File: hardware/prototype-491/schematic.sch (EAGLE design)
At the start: 10 parts

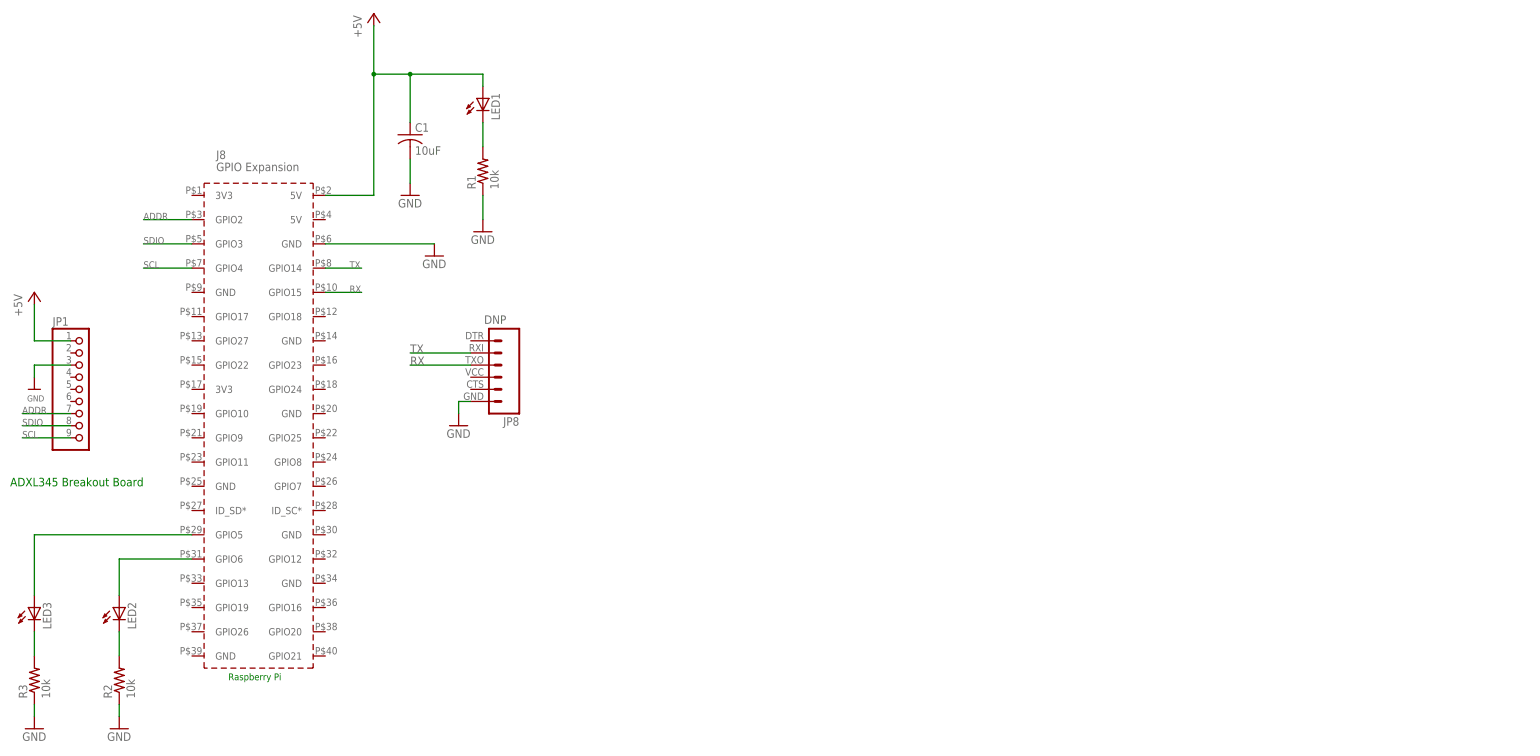
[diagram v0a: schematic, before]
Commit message: schematic completed
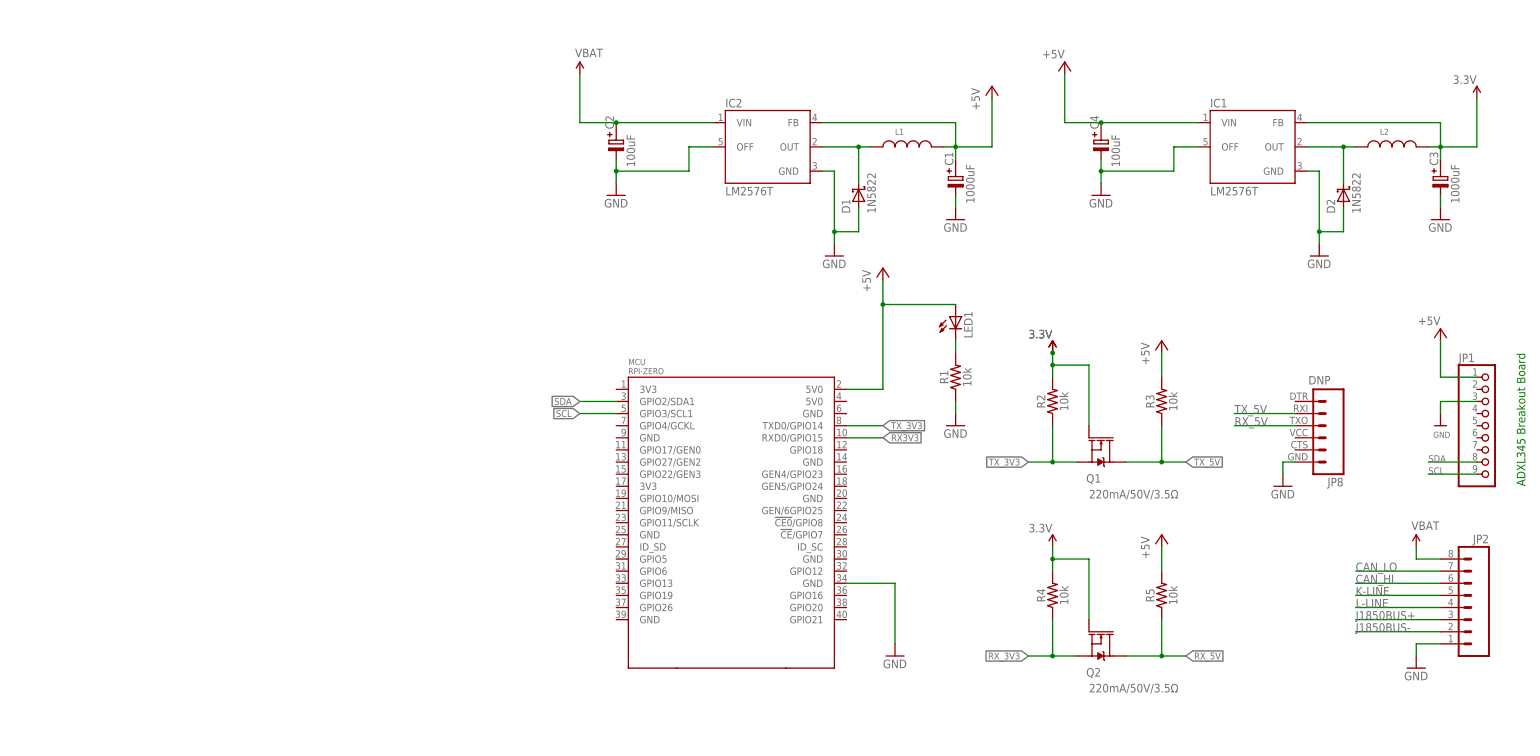
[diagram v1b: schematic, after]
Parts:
- removed LED2, LED3: (no value), adafruit:LED3MM
- removed RBPI: RPI3, e14_Rpi3_RevA:RPI3
- added C2, C4: 100uF, cap-pan40:C-PR-3,5X8
- added C3: 1000uF, cap-pan40:C-PR-3,5X8
- added D1, D2: 1N5822, 1N5822:1N5822
- added IC1, IC2: LM2576T, v-reg-3:LM2576T
- added JP2: (no value), SparkFun:M08BM08B-SRSS-TB
- added L1, L2: (no value), PowerMagnetics:WE-TI_1014_7447480101
- added MCU: RPI-ZERO, RPI-Zero:RPI-ZERO
- added Q1, Q2: 220mA/50V/3.5Ω, SparkFun-DiscreteSemi:MOSFET-NCH-BSS138
- added R4, R5: 10k, SparkFun-Resistors:10KOHM-HORIZ-1/4W-5%
- C1: value 10uF -> 1000uF; device adafruit:C-US050-025X075 -> cap-pan40:C-PR-3,5X8
- R1, R2, R3: device resistor:R-US_R0805 -> SparkFun-Resistors:10KOHM-HORIZ-1/4W-5%
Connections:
- removed net ADDR: JP1.7, RBPI.GPIO2
- removed net N$5: LED3.A, RBPI.GPIO5
- removed net N$6: LED3.C, R3.2
- removed net N$7: LED2.C, R2.2
- removed net RX: JP8.3, RBPI.GPIO15
- removed net SDIO: JP1.8, RBPI.GPIO3
- removed net TX: JP8.2, RBPI.GPIO14
- new net 3.3V: C3.+, IC1.FB, L2.2, Q1.G, Q2.G, R2.2, R4.2
- new net CAN_HI: JP2.6
- new net CAN_LO: JP2.7
- new net J1850BUS+: JP2.3
- new net J1850BUS-: JP2.2
- new net K-LINE: JP2.5
- new net L-LINE: JP2.4
- new net N$1: D2.C, IC1.OUT, L2.1
- new net RX3V3: MCU.RXD0/GPIO15
- new net RX_3V3: Q2.S, R4.1
- new net RX_5V: JP8.3, Q2.D, R5.1
- new net SDA: JP1.8, MCU.GPIO2/SDA1
- new net TX_3V3: MCU.TXD0/GPIO14, Q1.S, R2.1
- new net TX_5V: JP8.2, Q1.D, R3.1
- new net VBAT: JP2.8
- new net VCC: C2.+, IC2.VIN
- net +5V: now also C1.+, C4.+, IC1.VIN, IC2.FB, L1.2, MCU.5V0@1, R3.2, R5.2; no longer C1.1, RBPI.5V@2
- net GND: now also C1.-, C2.-, C3.-, C4.-, D1.A, D2.A, IC1.GND, IC1.OFF, IC2.GND, IC2.OFF, JP2.1, MCU.GND@7; no longer C1.2, R2.1, R3.1, RBPI.GND@6
- net N$4: now also D1.C, IC2.OUT, L1.1; no longer LED2.A, RBPI.GPIO6
- net SCL: now also MCU.GPIO3/SCL1; no longer RBPI.GPIO4
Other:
- note removed: "Raspberry Pi"
- moved on the sheet: JP1, JP8, LED1, R1, R2, R3

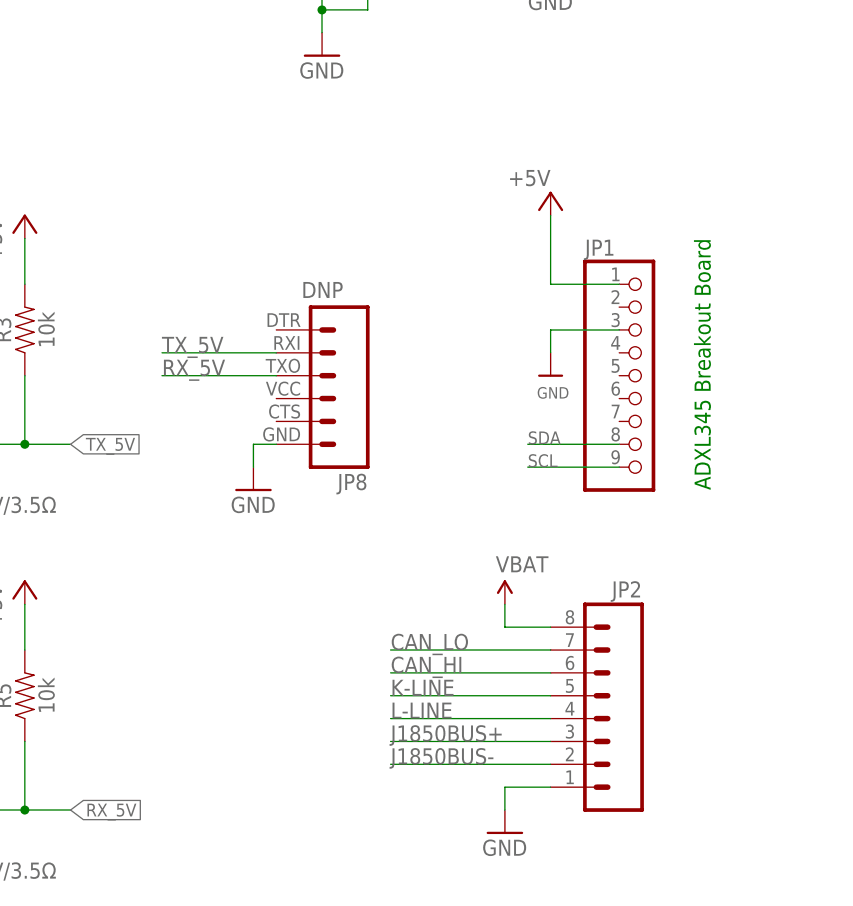
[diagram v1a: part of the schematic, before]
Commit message: changed a connector
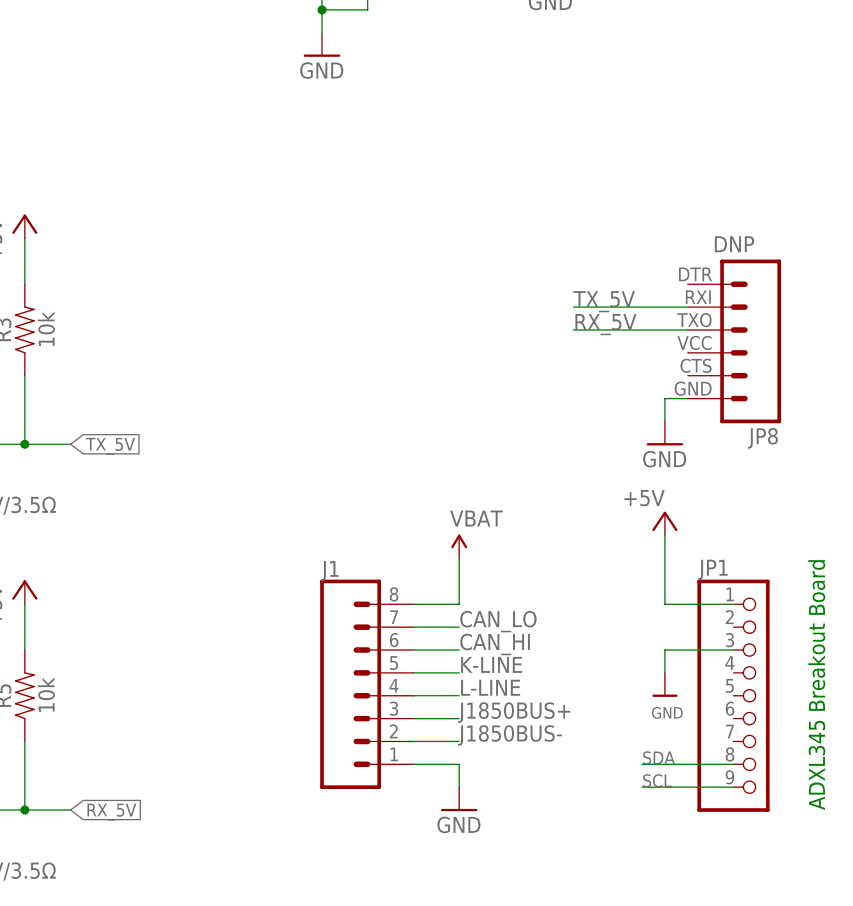
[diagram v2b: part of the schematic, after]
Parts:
- removed JP2: (no value), SparkFun:M08BM08B-SRSS-TB
- added J1: (no value), SparkFun-Connectors:CONN_08"
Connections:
- net CAN_HI: now also J1.6; no longer JP2.6
- net CAN_LO: now also J1.7; no longer JP2.7
- net GND: now also J1.1; no longer JP2.1
- net J1850BUS+: now also J1.3; no longer JP2.3
- net J1850BUS-: now also J1.2; no longer JP2.2
- net K-LINE: now also J1.5; no longer JP2.5
- net L-LINE: now also J1.4; no longer JP2.4
- net VBAT: now also J1.8; no longer JP2.8
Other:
- moved on the sheet: JP1, JP8

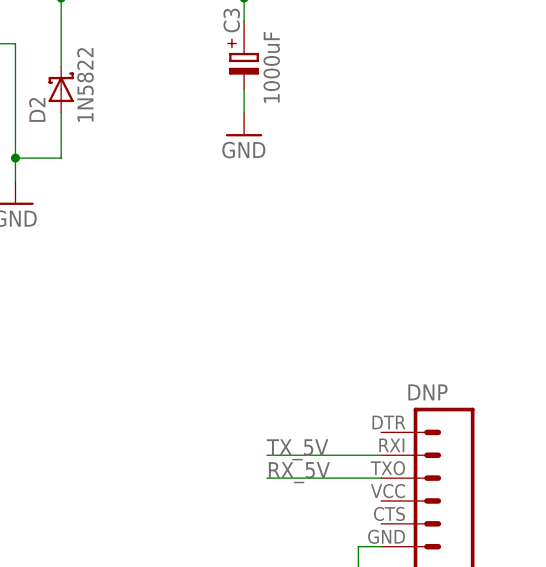
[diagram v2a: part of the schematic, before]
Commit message: routed signals
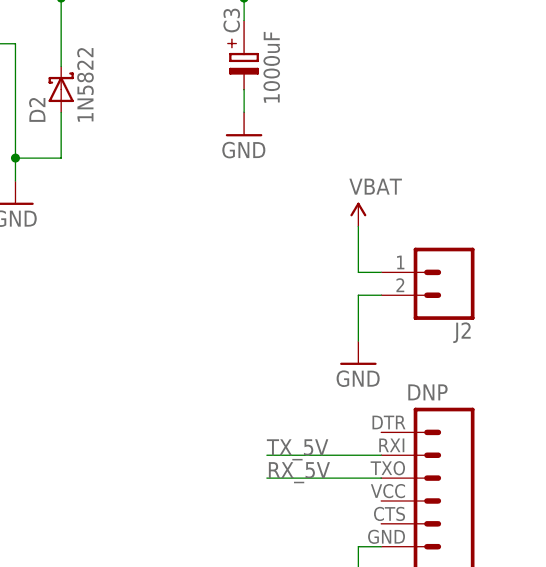
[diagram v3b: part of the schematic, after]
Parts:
- added J2: (no value), SparkFun-Connectors:CONN_02POLAR
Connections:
- net GND: now also J2.2
- net VCC: now also J2.1
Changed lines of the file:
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@@
 <setting verticaltext="up"/>
 </settings>
-<grid distance="0.1" unitdist="inch" unit="inch" style="dots" multiple="1" display="yes" altdistance="0.01" altunitdist="inch" altunit="inch"/>
+<grid distance="0.1" unitdist="inch" unit="inch" style="lines" multiple="1" display="no" altdistance="0.01" altunitdist="inch" altunit="inch"/>
 <layers>
 <layer number="1" name="Top" color="4" fill="1" visible="no" active="no"/>
@@
 </variantdefs>
 <classes>
-<class number="0" name="default" width="0" drill="0">
+<class number="0" name="default" width="0.3048" drill="0.508">
+<clearance class="0" value="0.3048"/>
 </class>
 </classes>
@@
 <part name="FRAME1" library="frames" library_urn="urn:adsk.eagle:library:229" deviceset="FRAME_A_L" device=""/>
 <part name="J1" library="SparkFun-Connectors" deviceset="CONN_08" device="&quot;"/>
+<part name="J2" library="SparkFun-Connectors" deviceset="CONN_02" device="POLAR"/>
+<part name="P+8" library="SparkFun" deviceset="VCC" device="" value="VBAT"/>
+<part name="GND9" library="SparkFun" deviceset="GND" device=""/>
 </parts>
 <sheets>
@@
 <attribute name="NAME" x="238.76" y="97.028" size="1.778" layer="95" font="vector"/>
 </instance>
+<instance part="J2" gate="G$1" x="287.02" y="147.32" smashed="yes" rot="R180">
+<attribute name="VALUE" x="289.56" y="152.146" size="1.778" layer="96" font="vector" rot="R180"/>
+<attribute name="NAME" x="289.56" y="141.732" size="1.778" layer="95" font="vector" rot="R180"/>
+</instance>
+<instance part="P+8" gate="1" x="276.86" y="152.4" smashed="yes">
+<attribute name="VALUE" x="275.844" y="155.956" size="1.778" layer="96"/>
+</instance>
+<instance part="GND9" gate="1" x="276.86" y="137.16" smashed="yes">
+<attribute name="VALUE" x="274.32" y="134.62" size="1.778" layer="96"/>
+</instance>
 </instances>
 <busses>
@@
 <wire x1="208.28" y1="177.8" x2="213.36" y2="177.8" width="0.1524" layer="91"/>
 <pinref part="C4" gate="G$1" pin="-"/>
+</segment>
+<segment>
+<pinref part="J2" gate="G$1" pin="2"/>
+<wire x1="279.4" y1="144.78" x2="276.86" y2="144.78" width="0.1524" layer="91"/>
+<wire x1="276.86" y1="144.78" x2="276.86" y2="139.7" width="0.1524" layer="91"/>
+<pinref part="GND9" gate="1" pin="GND"/>
 </segment>
 </net>
@@
 <junction x="91.44" y="182.88"/>
 </segment>
-</net>
+<segment>
+<pinref part="J2" gate="G$1" pin="1"/>
+<wire x1="279.4" y1="147.32" x2="276.86" y2="147.32" width="0.1524" layer="91"/>
+<wire x1="276.86" y1="147.32" x2="276.86" y2="152.4" width="0.1524" layer="91"/>
+<pinref part="P+8" gate="1" pin="VCC"/>
+</segment>
+</net>

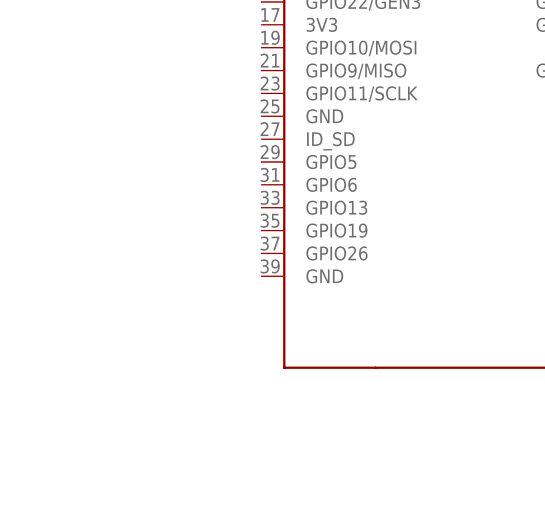
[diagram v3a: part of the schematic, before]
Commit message: added status LEDs to main board, completed board for CAN test module
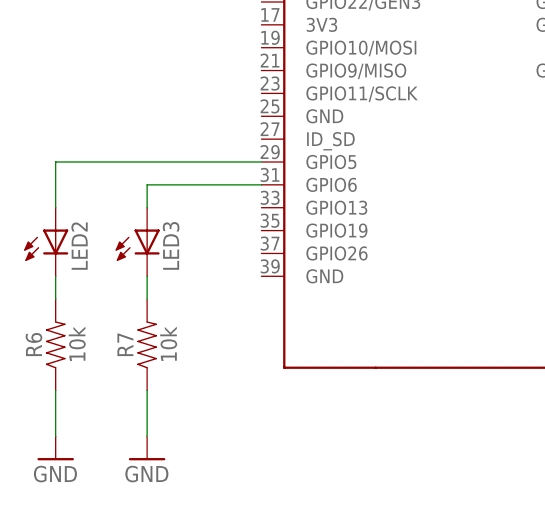
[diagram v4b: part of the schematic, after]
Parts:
- added LED2, LED3: (no value), adafruit:LED3MM
- added R6, R7: 10k, SparkFun-Resistors:10KOHM-HORIZ-1/4W-5%
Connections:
- new net N$2: LED2.A, MCU.GPIO5
- new net N$3: LED3.A, MCU.GPIO6
- new net N$5: LED2.C, R6.2
- new net N$6: LED3.C, R7.2
- net GND: now also R6.1, R7.1
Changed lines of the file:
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@@
 <part name="P+8" library="SparkFun" deviceset="VCC" device="" value="VBAT"/>
 <part name="GND9" library="SparkFun" deviceset="GND" device=""/>
+<part name="LED2" library="adafruit" library_urn="urn:adsk.eagle:library:420" deviceset="LED" device="3MM"/>
+<part name="LED3" library="adafruit" library_urn="urn:adsk.eagle:library:420" deviceset="LED" device="3MM"/>
+<part name="R6" library="SparkFun-Resistors" deviceset="10KOHM" device="-HORIZ-1/4W-5%" value="10k"/>
+<part name="R7" library="SparkFun-Resistors" deviceset="10KOHM" device="-HORIZ-1/4W-5%" value="10k"/>
+<part name="GND10" library="supply1" library_urn="urn:adsk.eagle:library:371" deviceset="GND" device=""/>
+<part name="GND11" library="supply1" library_urn="urn:adsk.eagle:library:371" deviceset="GND" device=""/>
 </parts>
 <sheets>
@@
 <attribute name="VALUE" x="274.32" y="134.62" size="1.778" layer="96"/>
 </instance>
+<instance part="LED2" gate="G$1" x="68.58" y="83.82" smashed="yes">
+<attribute name="NAME" x="72.136" y="79.248" size="1.778" layer="95" rot="R90"/>
+<attribute name="VALUE" x="74.295" y="79.248" size="1.778" layer="96" rot="R90"/>
+</instance>
+<instance part="LED3" gate="G$1" x="78.74" y="83.82" smashed="yes">
+<attribute name="NAME" x="82.296" y="79.248" size="1.778" layer="95" rot="R90"/>
+<attribute name="VALUE" x="84.455" y="79.248" size="1.778" layer="96" rot="R90"/>
+</instance>
+<instance part="R6" gate="G$1" x="68.58" y="71.12" smashed="yes" rot="R90">
+<attribute name="NAME" x="67.056" y="71.12" size="1.778" layer="95" font="vector" rot="R90" align="bottom-center"/>
+<attribute name="VALUE" x="70.104" y="71.12" size="1.778" layer="96" font="vector" rot="R90" align="top-center"/>
+</instance>
+<instance part="R7" gate="G$1" x="78.74" y="71.12" smashed="yes" rot="R90">
+<attribute name="NAME" x="77.216" y="71.12" size="1.778" layer="95" font="vector" rot="R90" align="bottom-center"/>
+<attribute name="VALUE" x="80.264" y="71.12" size="1.778" layer="96" font="vector" rot="R90" align="top-center"/>
+</instance>
+<instance part="GND10" gate="1" x="68.58" y="58.42" smashed="yes">
+<attribute name="VALUE" x="66.04" y="55.88" size="1.778" layer="96"/>
+</instance>
+<instance part="GND11" gate="1" x="78.74" y="58.42" smashed="yes">
+<attribute name="VALUE" x="76.2" y="55.88" size="1.778" layer="96"/>
+</instance>
 </instances>
 <busses>
@@
 <wire x1="276.86" y1="144.78" x2="276.86" y2="139.7" width="0.1524" layer="91"/>
 <pinref part="GND9" gate="1" pin="GND"/>
+</segment>
+<segment>
+<pinref part="R6" gate="G$1" pin="1"/>
+<wire x1="68.58" y1="66.04" x2="68.58" y2="60.96" width="0.1524" layer="91"/>
+<pinref part="GND10" gate="1" pin="GND"/>
+</segment>
+<segment>
+<pinref part="R7" gate="G$1" pin="1"/>
+<wire x1="78.74" y1="66.04" x2="78.74" y2="60.96" width="0.1524" layer="91"/>
+<pinref part="GND11" gate="1" pin="GND"/>
 </segment>
 </net>
@@
 </segment>
 </net>
+<net name="N$2" class="0">
+<segment>
+<pinref part="MCU" gate="G$1" pin="GPIO5"/>
+<wire x1="91.44" y1="91.44" x2="68.58" y2="91.44" width="0.1524" layer="91"/>
+<wire x1="68.58" y1="91.44" x2="68.58" y2="86.36" width="0.1524" layer="91"/>
+<pinref part="LED2" gate="G$1" pin="A"/>
+</segment>
+</net>
+<net name="N$3" class="0">
+<segment>
+<pinref part="MCU" gate="G$1" pin="GPIO6"/>
+<wire x1="91.44" y1="88.9" x2="78.74" y2="88.9" width="0.1524" layer="91"/>
+<wire x1="78.74" y1="88.9" x2="78.74" y2="86.36" width="0.1524" layer="91"/>
+<pinref part="LED3" gate="G$1" pin="A"/>
+</segment>
+</net>
+<net name="N$5" class="0">
+<segment>
+<pinref part="LED2" gate="G$1" pin="C"/>
+<wire x1="68.58" y1="78.74" x2="68.58" y2="76.2" width="0.1524" layer="91"/>
+<pinref part="R6" gate="G$1" pin="2"/>
+</segment>
+</net>
+<net name="N$6" class="0">
+<segment>
+<pinref part="LED3" gate="G$1" pin="C"/>
+<wire x1="78.74" y1="78.74" x2="78.74" y2="76.2" width="0.1524" layer="91"/>
+<pinref part="R7" gate="G$1" pin="2"/>
+</segment>
+</net>
